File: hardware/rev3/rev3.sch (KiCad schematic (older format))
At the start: 0 parts

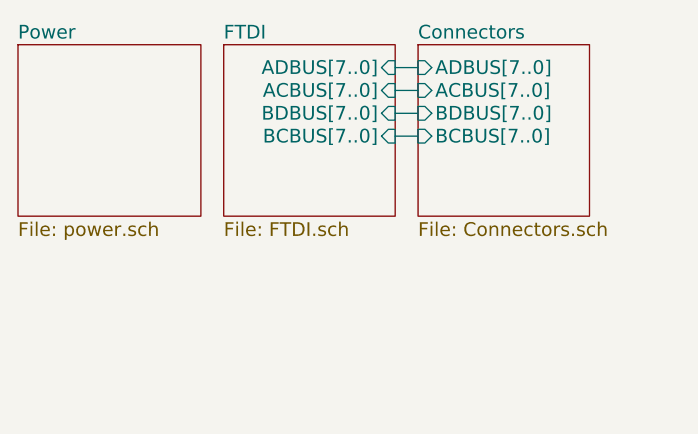
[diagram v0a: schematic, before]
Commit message: Add AD9102 to the schematic.
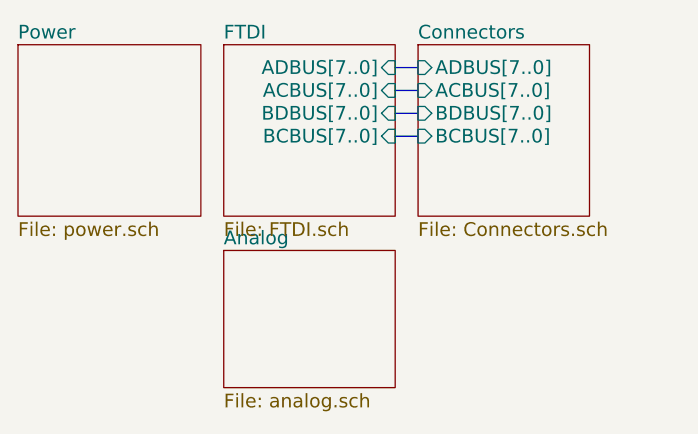
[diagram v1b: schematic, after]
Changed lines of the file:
@@
 LIBS:valves
 LIBS:ftdi
+LIBS:analog_devices
+LIBS:AD9102
+LIBS:LMK61XX
 LIBS:rev3-cache
 EELAYER 25 0
@@
 $Descr A4 11693 8268
 encoding utf-8
-Sheet 1 4
+Sheet 1 5
 Title ""
 Date ""
@@
 Wire Bus Line
 	2400 1100 2300 1100
+$Sheet
+S 1550 1600 750  600
+U 58FBEC6E
+F0 "Analog" 60
+F1 "analog.sch" 60
+$EndSheet
 $EndSCHEMATC
